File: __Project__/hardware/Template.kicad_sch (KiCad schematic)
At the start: 0 parts

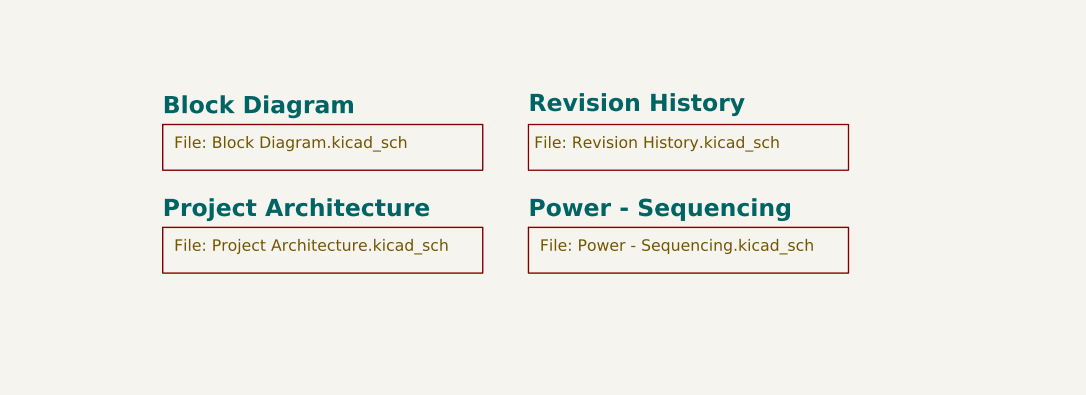
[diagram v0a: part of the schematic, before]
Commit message: Add Power and interface topology pages to KiBot template
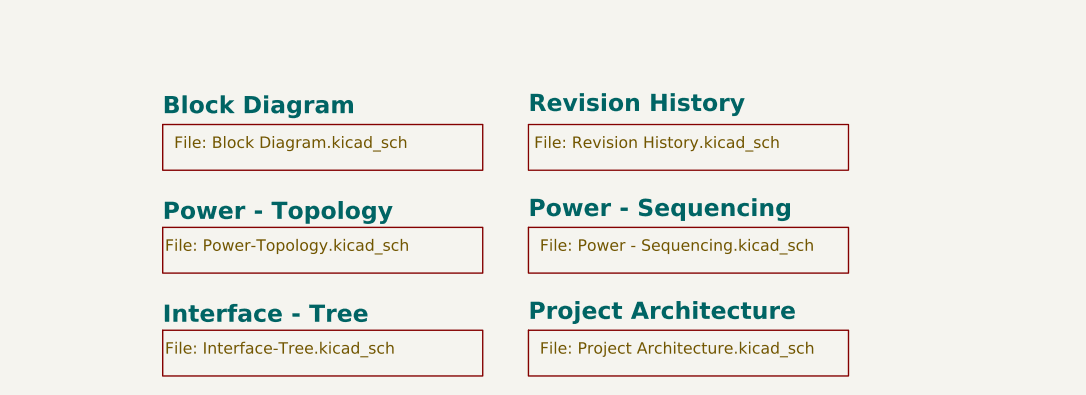
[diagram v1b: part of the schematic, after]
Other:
- added sheet Interface - Tree (Interface-Tree.kicad_sch)
- added sheet Power - Topology (Power-Topology.kicad_sch)
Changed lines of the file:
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@@
+	)
+	(sheet
+		(at 306.07 326.39)
+		(size 35.56 5.08)
+		(exclude_from_sim no)
+		(in_bom yes)
+		(on_board yes)
+		(dnp no)
+		(stroke
+			(width 0.1524)
+			(type solid)
+		)
+		(fill
+			(color 0 0 0 0.0000)
+		)
+		(property "Sheetname" "Interface - Tree"
+			(at 306.07 325.6784 0)
+			(effects
+				(font
+					(face "Times New Roman")
+					(size 1.905 1.905)
+					(thickness 0.3556)
+					(bold yes)
+					(color 0 0 0 1)
+				)
+				(justify left bottom)
+			)
+		)
+		(property "Sheetfile" "Interface-Tree.kicad_sch"
+			(at 306.324 327.66 0)
+			(effects
+				(font
+					(size 1.27 1.27)
+				)
+				(justify left top)
+			)
+		)
+		(instances
+			(project "Template"
+				(path "/d5742f03-3b1a-42e5-a384-018bd4b919aa"
+					(page "5")
+				)
+			)
+		)
 	)
 	(sheet
@@
 			(project "Template"
 				(path "/d5742f03-3b1a-42e5-a384-018bd4b919aa"
-					(page "7")
+					(page "4")
 				)
 			)
@@
 			(project "Template"
 				(path "/d5742f03-3b1a-42e5-a384-018bd4b919aa"
-					(page "6")
+					(page "9")
 				)
 			)
@@
 	)
 	(sheet
+		(at 346.71 326.39)
+		(size 35.56 5.08)
+		(exclude_from_sim no)
+		(in_bom yes)
+		(on_board yes)
+		(dnp no)
+		(stroke
+			(width 0.1524)
+			(type solid)
+		)
+		(fill
+			(color 0 0 0 0.0000)
+		)
+		(property "Sheetname" "Project Architecture"
+			(at 346.71 325.3609 0)
+			(effects
+				(font
+					(face "Times New Roman")
+					(size 1.905 1.905)
+					(bold yes)
+					(color 0 0 0 1)
+				)
+				(justify left bottom)
+			)
+		)
+		(property "Sheetfile" "Project Architecture.kicad_sch"
+			(at 347.98 327.66 0)
+			(effects
+				(font
+					(face "Arial")
+					(size 1.27 1.27)
+				)
+				(justify left top)
+			)
+		)
+		(instances
+			(project "KDT_Hierarchical_KiBot"
+				(path "/f9e05184-c88b-4a88-ae9c-ab2bdb32be7c"
+					(page "3")
+				)
+			)
+			(project "Template"
+				(path "/d5742f03-3b1a-42e5-a384-018bd4b919aa"
+					(page "6")
+				)
+			)
+		)
+	)
+	(sheet
 		(at 306.07 314.96)
 		(size 35.56 5.08)
@@
 			(color 0 0 0 0.0000)
 		)
-		(property "Sheetname" "Project Architecture"
-			(at 306.07 313.9309 0)
-			(effects
-				(font
-					(face "Times New Roman")
-					(size 1.905 1.905)
-					(bold yes)
-					(color 0 0 0 1)
-				)
-				(justify left bottom)
-			)
-		)
-		(property "Sheetfile" "Project Architecture.kicad_sch"
-			(at 307.34 316.23 0)
-			(effects
-				(font
-					(face "Arial")
-					(size 1.27 1.27)
-				)
-				(justify left top)
-			)
-		)
-		(instances
-			(project "KDT_Hierarchical_KiBot"
-				(path "/f9e05184-c88b-4a88-ae9c-ab2bdb32be7c"
-					(page "3")
-				)
-			)
+		(property "Sheetname" "Power - Topology"
+			(at 306.07 314.2484 0)
+			(effects
+				(font
+					(face "Times New Roman")
+					(size 1.905 1.905)
+					(thickness 0.3556)
+					(bold yes)
+					(color 0 0 0 1)
+				)
+				(justify left bottom)
+			)
+		)
+		(property "Sheetfile" "Power-Topology.kicad_sch"
+			(at 306.324 316.23 0)
+			(effects
+				(font
+					(size 1.27 1.27)
+				)
+				(justify left top)
+			)
+		)
+		(instances
 			(project "Template"
 				(path "/d5742f03-3b1a-42e5-a384-018bd4b919aa"
@@
 	)
 	(embedded_fonts no)
-	(embedded_files
-		(file
-			(name "KDT_Template_GIT.kicad_wks")
-			(type worksheet)
-			(data |KLUv/WCOH90hADbldCEA0zz8vwV4dA49qrdgbG9UWNWEsQ8RBFilMbXZ//+TKl5pAGcAawB8j718
-				+vQ7v/2UpMfm1X3E3Ny978pmd8wlc1pf5wu/ptgtuJyuStHHdDJ7sM7ldFH1cSif/YM7AQAIbDgd
-				n5TKJFHiu2cSi+VGer775VjjCwEQmLJaa2Wpfb3zyXGHAAicGo9I3jFrCAH1MVufPn2+yz2S5a78
-				dFF2kvQ19/ce7P2JzRxKj8drsZRSqvAFaiQQDTjnII67xuODLLmfnMxlv24gez2tVCq0VgSA3pb6
-				l/1zb6Qqff/gXukXrS779ApMoA8fdbbfL97gp09qzLEOIy30uMcDgqD1bVbg2INHXLglRE4Cgl2t
-				zOt9H3Fm80hV9ZvAbGHkQTqwm3AfparVO5+5g7/KYlajqq22siwdfVxki1QLh3LhrXq9llkUZtnX
-				ZSepvJlvll4Ura9lmkEi83eMMaD0XWPT3GOBCUOAIgPcGGLYLTQNw5yX8T0vbJZZtLL15BxhF2L6
-				jYwY4RYJOY4BWtRllT2HuMyKgiUmvg1ywMQQwTUgH8XbIiB9N+ZGYKPQ27pvm1iW1fXN/E5IfveB
-				1so9No9zdApb68d5iw7kEvqST2wphmEBgP6o4SVDJTIjKUkhbQZQhAjJWJEdEgDBEAZFEAxhGJZC
-				EAzBKAYJ44wRECJoiFBA6wHhizrKqI2WoRGqJst81kW3E7qPTqq+VxKtbeMJC1W8PBrl5rVIdXR3
-				fbWSaYOeQK42nKPAMXrQnlrHIVvD2uamNJqrapdu2IjRqFedDa/rYYhRjIsKv8kkwUHYwRrmzIEy
-				x3jkBh/9dS1+990fuIQYsiQzu0jjib3lu9fEGcfbTm9qf26AfYrwXHBwyw+drVyLsaTFskuBxI/k
-				oKeJFy3zvOIwbbEWPa6fOEZgmhbCEPaia/5AWVsIvf0W/OGnkyve17TyW8ggGkLScP5G8ADr2/Pm
-				0tykbcl+ZFCkWqSmZVMKudto9Y6tibFrJCTiTSfUxvafVIicgJTVHNVGRKZALL9Gqs+OCq+dG6dH
-				JzmRSXo4oyMtTnlmrl/prZE4TukAy9cYy+h3cACCxbDQuzle6c1YBqzKbGDHC32YnSWNhamDuwwF
-				RBp2m5E1lIPIzlWhZcddNe4fxhmuzRknOohgSepQ3q2F8HoDfoAY2TOFhbQIE+IW3tCTIDSlYF4y
-				lnQjLQshsBPQxB/jnEk35EMHtySbLzk+F8MRbmw7jMhcOdacNnQOdNAJAI/Rls5ICgJvgonReU+r
-				kDYqB5pqGPM+zs+NOsilXcAr0JGGUqIPechLGJGXWZHNLjt8kKmKv6CjInHBhBPAvq3h9ruQ9xVh
-				c8CPcRBhCS0DuChaYtg2iHcpxN7Dfns7Uwnwgg2I8XfHpGGpMxhCs0nmwoipez/UY7nqU2GZgs/C
-				D78HSbu2jaWvCg==|
-			)
-			(checksum "DB3DC728C2AEB6FD5D8E1CEB972FF7A3")
-		)
-	)
 )

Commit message: Update project template
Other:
- sheet Power - Topology: file Power-Topology.kicad_sch -> Power - Topology.kicad_sch
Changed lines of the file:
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@@
 			)
 		)
-		(property "Sheetfile" "Power-Topology.kicad_sch"
+		(property "Sheetfile" "Power - Topology.kicad_sch"
 			(at 306.324 316.23 0)
 			(effects
